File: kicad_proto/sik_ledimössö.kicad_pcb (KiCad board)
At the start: 2 copper layers, 174.5 x 255.1 mm, 76 parts, among them J1 Conn_01x06_Pin, J2 Conn_01x02_Pin, U1 ATtiny861A-S

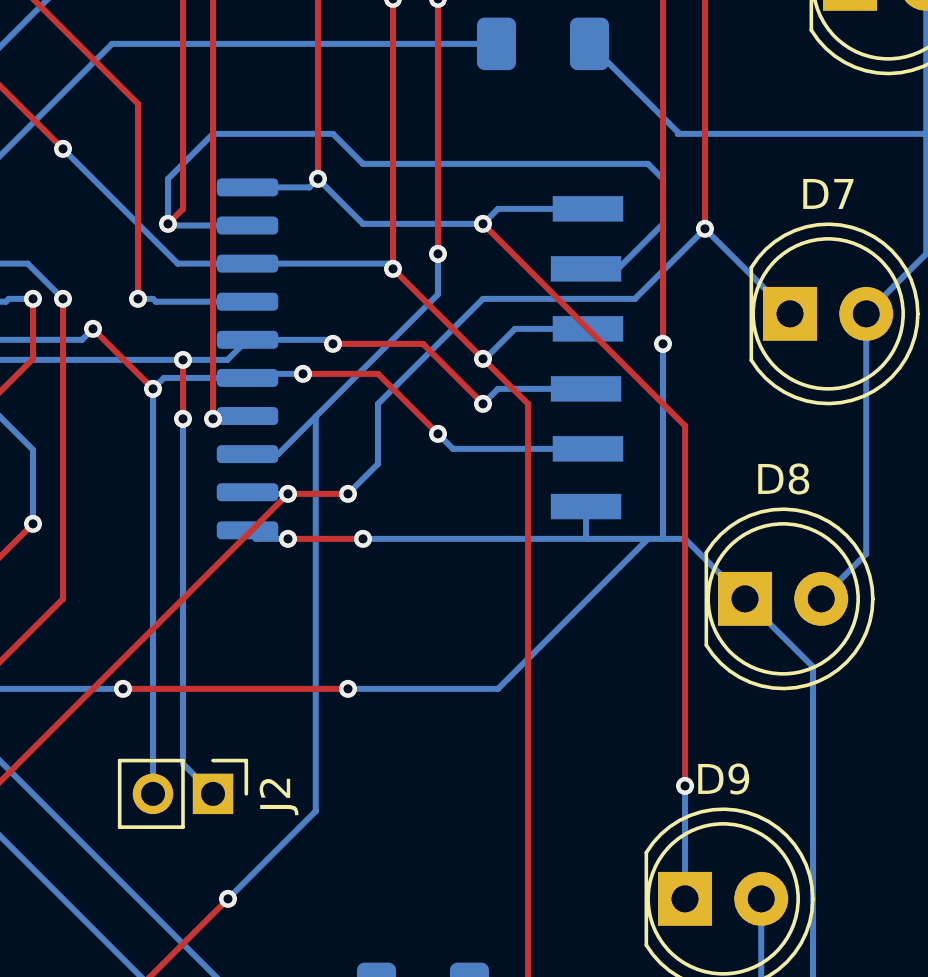
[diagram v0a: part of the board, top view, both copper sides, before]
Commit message: Edistystä*
Paremman leiskan teko aloitettu.

Alustavat koodit valmiina.
Osa kopsattu ja muokattu Elektroniikkakerhon LED-merkki reposta.

Protolevy kokoonpanossa.
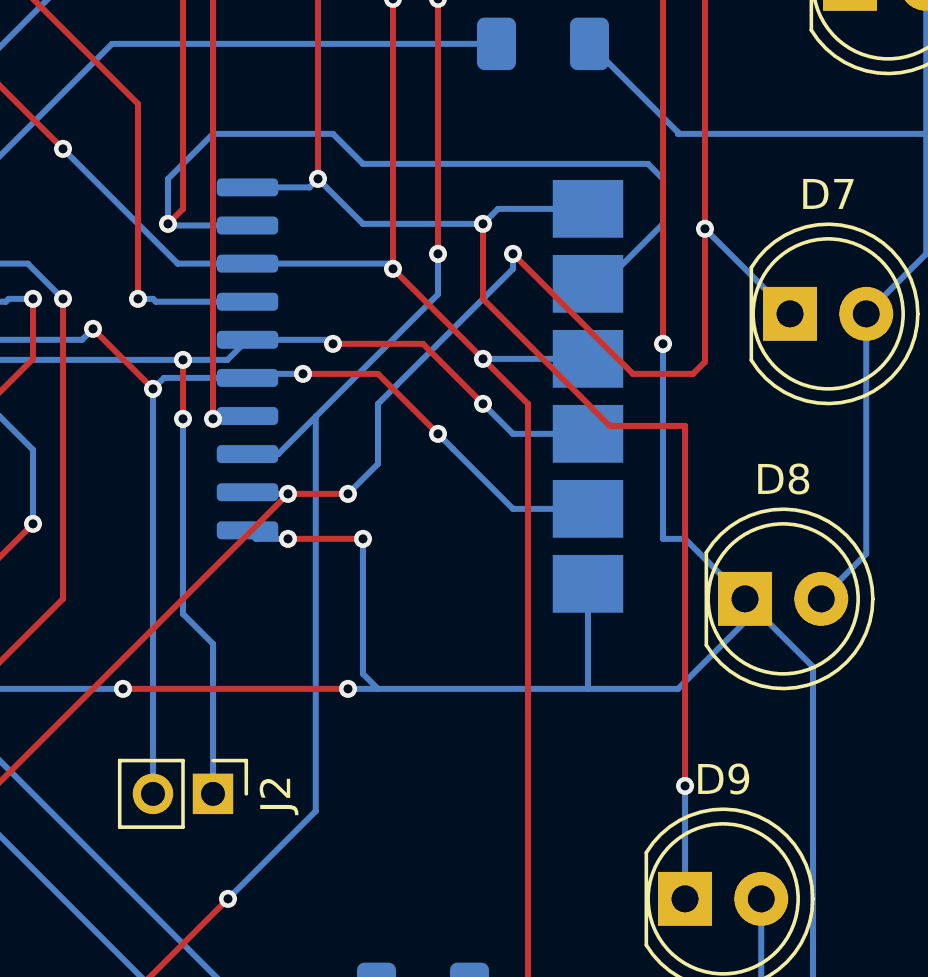
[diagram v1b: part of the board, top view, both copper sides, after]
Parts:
- moved J1 0.49 mm to (128.5, 89.0)
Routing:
- net Net-(D15-K): track 434.2 -> 440.4 mm, vias 17 -> 18
- net Net-(D1-K): track 448.5 -> 450.0 mm
- net GND: track 43.4 -> 44.2 mm
